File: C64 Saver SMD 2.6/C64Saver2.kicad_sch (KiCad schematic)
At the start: 24 parts, among them J1 Conn_01x04, J2 Conn_01x08, J4 Conn_01x08, J5 Conn_01x04, J6 Conn_01x04, Q1 BC847, Q2 IRFR5305, U1 TL431DBZ

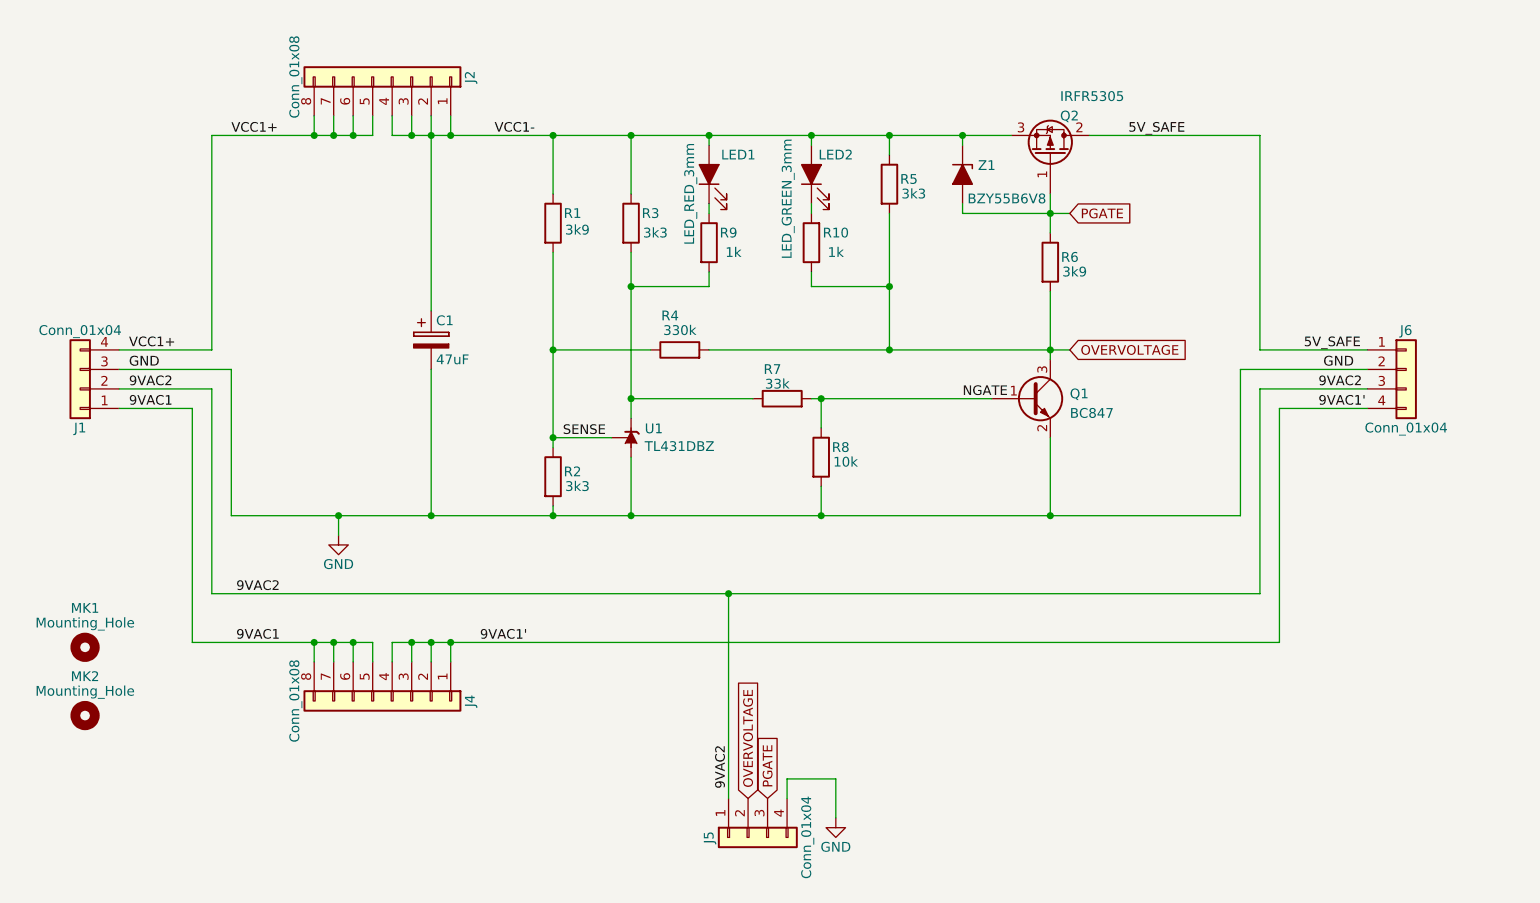
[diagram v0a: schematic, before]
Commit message: layout for tht 2.6. added connector for leds as alternative to smd leds
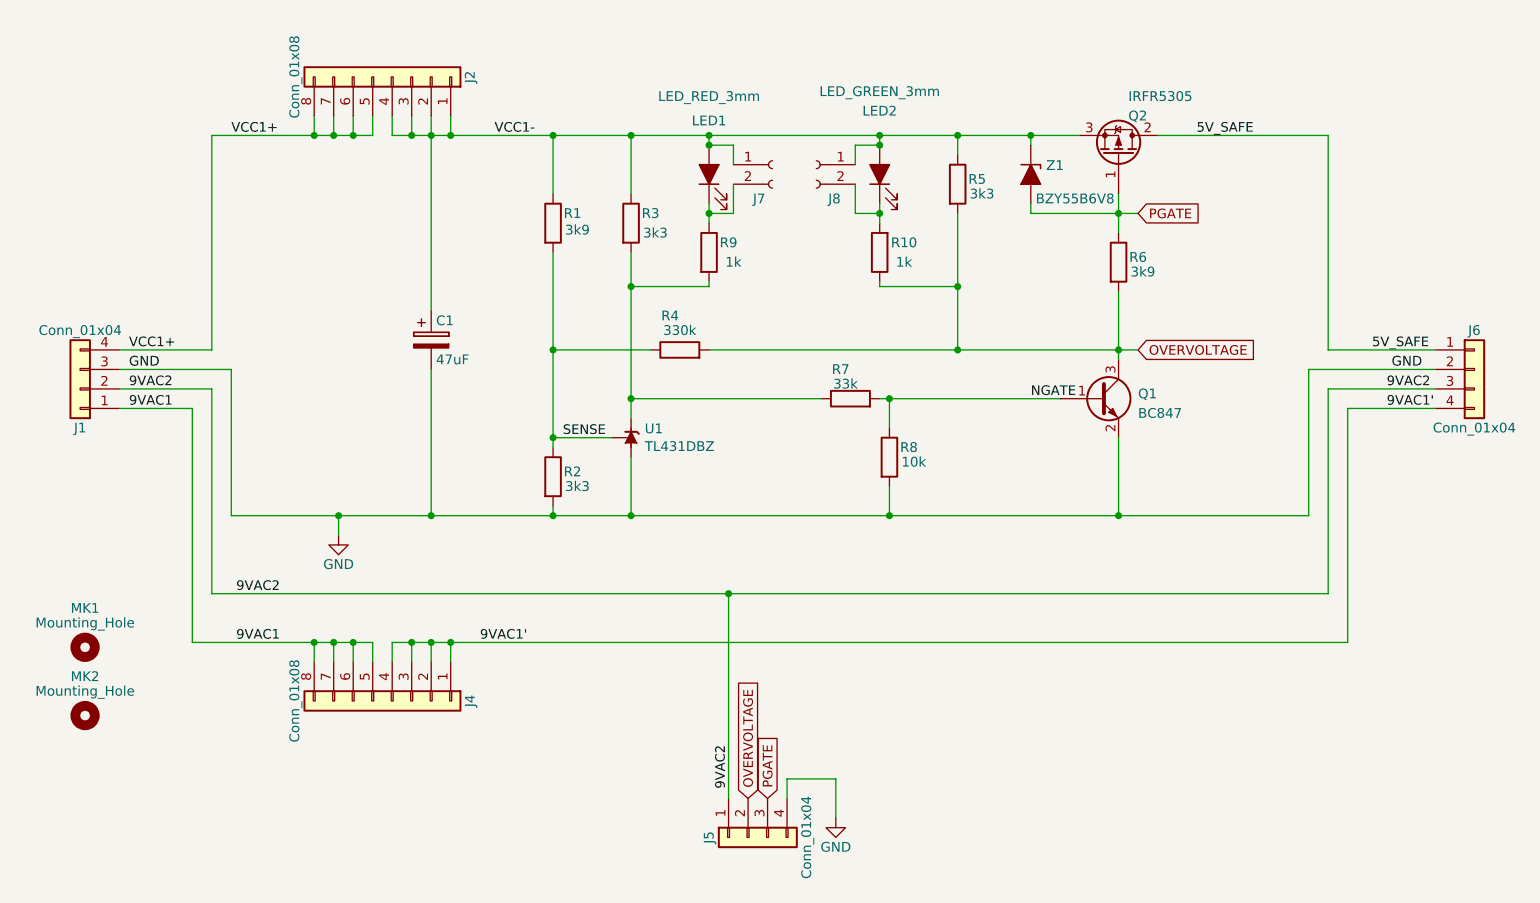
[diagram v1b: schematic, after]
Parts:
- added J7, J8: Conn_01x02_Socket, Connector_PinHeader_2.54mm:PinHeader_1x02_P2.54mm_Vertical, symbol Connector:Conn_01x02_Socket
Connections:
- net VCC1-: now also J7.1 (Pin_1), J8.1 (Pin_1)
- net at LED1.1 (K), R9.1: now also J7.2 (Pin_2)
- net at LED2.1 (K), R10.2: now also J8.2 (Pin_2)
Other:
- moved on the sheet: J6, LED2, Q1, Q2, R10, R5, R6, R7, R8, R9, Z1

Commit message: Preparing for Saver 2.6, moving 2.5 and 2.4 to oldfiles folder
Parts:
- MK1, MK2: now left out of the parts list
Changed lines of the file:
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@@
   (title_block
     (title "C64 Saver 2 SMD")
-    (date "2023-03-20")
+    (date "2023-03-26")
     (rev "2.6")
   )
@@
   (symbol (lib_id "C64Saver2-rescue:CP") (at 76.835 91.44 0) (unit 1)
     (in_bom yes) (on_board yes) (dnp no)
-    (property "Reference" "C1" (at 77.47 88.9 0)
+    (property "Reference" "C1" (at 80.01 90.17 0)
       (effects (font (size 1.27 1.27)) (justify left))
     )
-    (property "Value" "47uF" (at 77.47 93.98 0)
+    (property "Value" "47uF" (at 80.01 93.345 0)
       (effects (font (size 1.27 1.27)) (justify left))
     )
@@
       (effects (font (size 1.27 1.27)))
     )
-    (property "Value" "3k9" (at 95.885 77.089 0)
+    (property "Value" "3k9" (at 95.885 77.47 0)
       (effects (font (size 1.27 1.27)))
     )
@@
   (symbol (lib_id "C64Saver2-rescue:R") (at 92.71 109.22 0) (unit 1)
     (in_bom yes) (on_board yes) (dnp no)
-    (property "Reference" "R2" (at 95.25 108.585 0)
+    (property "Reference" "R2" (at 95.25 107.95 0)
       (effects (font (size 1.27 1.27)))
     )
@@
   (symbol (lib_id "C64Saver2-rescue:R") (at 166.37 81.28 0) (unit 1)
     (in_bom yes) (on_board yes) (dnp no)
-    (property "Reference" "R6" (at 168.91 80.645 0)
+    (property "Reference" "R6" (at 168.91 80.01 0)
       (effects (font (size 1.27 1.27)))
     )
@@
   (symbol (lib_id "C64Saver2-rescue:R") (at 145.415 71.12 0) (unit 1)
     (in_bom yes) (on_board yes) (dnp no)
-    (property "Reference" "R5" (at 147.955 70.485 0)
+    (property "Reference" "R5" (at 147.955 69.85 0)
       (effects (font (size 1.27 1.27)))
     )
@@
   )
   (symbol (lib_id "C64Saver2-rescue:Mounting_Hole") (at 31.75 131.445 0) (unit 1)
-    (in_bom yes) (on_board yes) (dnp no)
+    (in_bom no) (on_board yes) (dnp no)
     (property "Reference" "MK1" (at 31.75 126.365 0)
       (effects (font (size 1.27 1.27)))
@@
   )
   (symbol (lib_id "C64Saver2-rescue:Mounting_Hole") (at 31.75 140.335 0) (unit 1)
-    (in_bom yes) (on_board yes) (dnp no)
+    (in_bom no) (on_board yes) (dnp no)
     (property "Reference" "MK2" (at 31.75 135.255 0)
       (effects (font (size 1.27 1.27)))
@@
   (symbol (lib_id "C64Saver2-rescue:Conn_01x08") (at 71.755 57.15 270) (mirror x) (unit 1)
     (in_bom yes) (on_board yes) (dnp no)
-    (property "Reference" "J2" (at 81.915 57.15 0)
-      (effects (font (size 1.27 1.27)))
-    )
+    (property "Reference" "J2" (at 81.915 57.15 90)
+      (effects (font (size 1.27 1.27)))
+    )

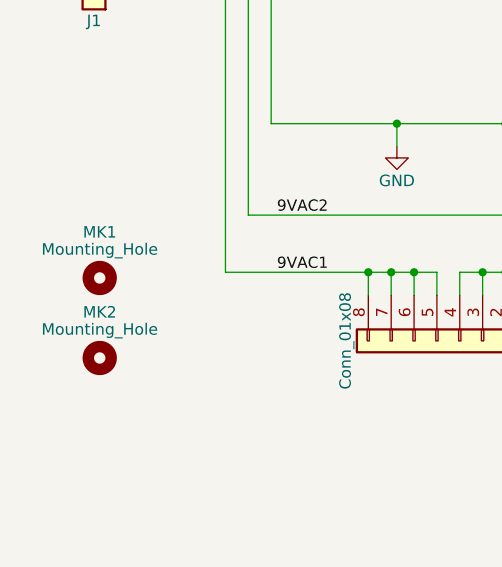
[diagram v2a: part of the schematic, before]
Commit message: added digi-key order numbers to ibom
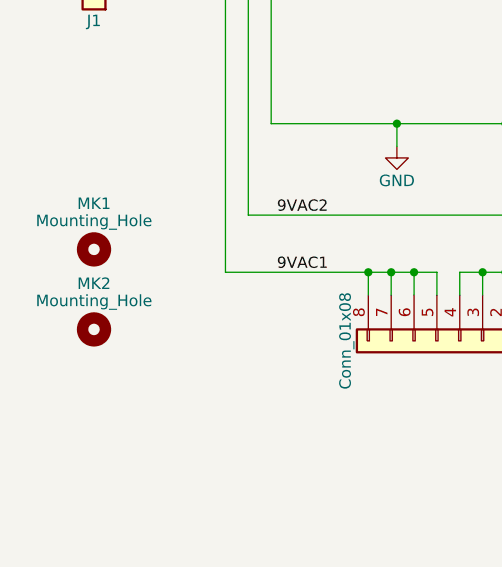
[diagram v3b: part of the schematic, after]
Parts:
- C1: Digi-Key (none) -> 493-3935-1-ND
- J1, J2, J4, J5, J6: comment (none) -> optional
- J7, J8: comment (none) -> optional; now left out of the parts list
- LED1: Digi-Key (none) -> 160-1956-ND; comment (none) -> SMD or THT. but not both
- LED2: Digi-Key (none) -> 160-1142-ND; comment (none) -> SMD or THT. but not both
- Q1: Digi-Key (none) -> 1727-2921-1-ND
- Q2: Digi-Key (none) -> IRFR5305TRLPBFCT-ND
- R1, R6: Digi-Key (none) -> P3.90KCCT-ND
- R10, R9: Digi-Key (none) -> P1.00KCCT-ND
- R2, R3, R5: Digi-Key (none) -> P3.30KCCT-ND
- R4: Digi-Key (none) -> P330KCCT-ND
- R7: Digi-Key (none) -> P33.0KCCT-ND
- R8: Digi-Key (none) -> P10.0KCCT-ND
- U1: Digi-Key (none) -> 296-26721-1-ND
- Z1: Digi-Key (none) -> 1727-3668-1-ND
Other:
- moved on the sheet: MK1, MK2

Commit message: updated schematics pdfs
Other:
- note added: "Choose 0805 SMD LEDs or 3mm T1 throughhole LEDs, but not both."
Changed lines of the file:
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@@
   (title_block
     (title "C64 Saver 2 SMD")
-    (date "2023-03-26")
+    (date "2023-04-02")
     (rev "2.6")
   )
@@
     (stroke (width 0) (type default))
   )
+  (text "Choose 0805 SMD LEDs or 3mm T1 throughhole LEDs, but not both."
+    (at 93.98 51.435 0)
+    (effects (font (size 1.27 1.27)) (justify left bottom))
+  )
   (label "9VAC1" (at 51.435 130.81 0) (fields_autoplaced)
